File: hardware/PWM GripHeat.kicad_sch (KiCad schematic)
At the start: 21 parts, among them J1 Screw_Terminal_01x02, J2 Screw_Terminal_01x02, Q1 SiS415DNT, Q2 2N7002H

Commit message: Getting there
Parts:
- removed C1, C2, C3, C4, C5: 10uF, Capacitor_SMD:C_0805_2012Metric_Pad1.18x1.45mm_HandSolder, symbol Device:C
- removed C6, C7: EMK325ABJ107MM-T, Capacitor_SMD:C_1210_3225Metric_Pad1.33x2.70mm_HandSolder, symbol Device:C
- removed D1: BZV55B18, Diode_SMD:D_MiniMELF, symbol Diode:BZV55B18
- removed D2: SMAJ24CA, Diode_SMD:D_SMA, symbol Diode:SMAJ24CA
- removed D3: B360, Diode_SMD:D_SMC, symbol Diode:B360
- removed F1: Polyfuse_Small, Fuse:Fuse_2920_7451Metric_Pad2.10x5.45mm_HandSolder, symbol Device:Polyfuse_Small
- removed J2: Screw_Terminal_01x02, TerminalBlock_Phoenix:TerminalBlock_Phoenix_MKDS-1,5-2-5.08_1x02_P5.08mm_Horizontal, symbol Connector:Screw_Terminal_01x02
- removed L1, L2: 100uH, Inductor_SMD:L_Bourns_SRR1260, symbol Device:L
- removed PS1: LM2576HVS-5, Package_TO_SOT_SMD:TO-263-5_TabPin3, symbol Regulator_Switching:LM2576HVS-5
- removed Q1: SiS415DNT, Package_SO:Vishay_PowerPAK_1212-8_Single, symbol Transistor_FET:SiS415DNT
- removed Q2: 2N7002H, Package_TO_SOT_SMD:SOT-23, symbol Transistor_FET:2N7002H
- removed R1: 2.2k, Resistor_SMD:R_1206_3216Metric_Pad1.30x1.75mm_HandSolder, symbol Device:R
- removed R2: 100k, Resistor_SMD:R_1206_3216Metric_Pad1.30x1.75mm_HandSolder, symbol Device:R
- added C10, C12, C8, C9: 10uF, Capacitor_SMD:C_0805_2012Metric_Pad1.18x1.45mm_HandSolder, symbol Device:C
- added C11, C14: 10nF, Capacitor_SMD:C_0805_2012Metric_Pad1.18x1.45mm_HandSolder, symbol Device:C
- added D10, D4, D8, D9: BZV55B5V1, Diode_SMD:D_MiniMELF, symbol Diode:BZV55B5V1
- added D5, D6, D7: BZV55B18, Diode_SMD:D_MiniMELF, symbol Diode:BZV55B18
- added J2: 1770898, TerminalBlock_Phoenix:TerminalBlock_Phoenix_PTSM-0,5-3-2.5-H-THR_1x03_P2.50mm_Horizontal, symbol Connector:Screw_Terminal_01x03
- added J4: 1770924, TerminalBlock_Phoenix:TerminalBlock_Phoenix_PTSM-0,5-6-2.5-H-THR_1x06_P2.50mm_Horizontal, symbol Connector:Screw_Terminal_01x06
- added J5: 0878340619, Connector_IDC:IDC-Header_2x03_P2.54mm_Vertical, symbol Connector_Generic:Conn_02x03_Odd_Even
- added R10, R11: 100k, Resistor_SMD:R_0805_2012Metric_Pad1.20x1.40mm_HandSolder, symbol Device:R
- added R12, R13, R14: 470k, Resistor_SMD:R_0805_2012Metric_Pad1.20x1.40mm_HandSolder, symbol Device:R
- added R4: 100k, Resistor_SMD:R_1206_3216Metric_Pad1.30x1.75mm_HandSolder, symbol Device:R
- added R5, R6, R7, R8: 100R, Resistor_SMD:R_0805_2012Metric_Pad1.20x1.40mm_HandSolder, symbol Device:R
- added R9: 1k, Resistor_SMD:R_0805_2012Metric_Pad1.20x1.40mm_HandSolder, symbol Device:R
- added TP4: SW_IN, TestPoint:TestPoint_Pad_D1.5mm, symbol Connector:TestPoint
- added TP5: RED, TestPoint:TestPoint_Pad_D1.5mm, symbol Connector:TestPoint
- added TP6: GREEN, TestPoint:TestPoint_Pad_D1.5mm, symbol Connector:TestPoint
- added TP7: BLUE, TestPoint:TestPoint_Pad_D1.5mm, symbol Connector:TestPoint
- added TP8: TestPoint, TestPoint:TestPoint_Pad_D1.5mm, symbol Connector:TestPoint
- added U1: ATtiny85-20P, Package_DIP:DIP-8_W7.62mm, symbol MCU_Microchip_ATtiny:ATtiny85-20P
- added U2: SiA462DJ, Package_TO_SOT_SMD:Vishay_PowerPAK_SC70-6L_Single, symbol Transistor_FET:SiA462DJ
- added U3: LM324, Package_SO:SOIC-14_3.9x8.7mm_P1.27mm, symbol Amplifier_Operational:LM324
- J1: value Screw_Terminal_01x02 -> 1770885; footprint TerminalBlock_Phoenix:TerminalBlock_Phoenix_MKDS-1,5-2-5.08_1x02_P5.08mm_Horizontal -> TerminalBlock_Phoenix:TerminalBlock_Phoenix_PTSM-0,5-2-2.5-H-THR_1x02_P2.50mm_Horizontal
- R3: value 100k -> 470k; footprint Resistor_SMD:R_1206_3216Metric_Pad1.30x1.75mm_HandSolder -> Resistor_SMD:R_0805_2012Metric_Pad1.20x1.40mm_HandSolder
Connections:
- net +5V: now also C10.2, C11.2, C12.2, C9.2, J5.2 (Pin_2), R10.1, U1.8 (VCC), U3.4 (V+)
- net +BATT: now also J1.1 (Pin_1), R9.1
- net GND: now also C10.1, C11.1, C12.1, C14.1, C8.1, C9.1, D10.2 (A), D4.2 (A), D5.2 (A), D6.2 (A), D7.2 (A), D8.2 (A), D9.2 (A), J2.3 (Pin_3), J4.6 (Pin_6), J5.6 (Pin_6), R11.2, R4.2, U1.4 (GND), U2.4 (S), U3.11 (V-); no longer R3.2
- net at J1.2 (Pin_2): now also D7.1 (K), U2.1 (D)
- net +IGN renamed +2V5
- net +2V5: now also C14.2, R10.2, R11.1, R12.1, R13.1, R14.2, U3.10 (+), U3.12 (+), U3.3 (+), U3.5 (+)
- new net: D4.1 (K), R13.2, R5.1, U3.14
- new net: D10.1 (K), R12.2, R7.1, U3.7
- new net: J4.5 (Pin_5), R5.2
- new net: D9.1 (K), R3.2, R6.1, U3.8
- new net: C8.2, D6.1 (K), R8.1, U3.2 (-)
- new net: J4.2 (Pin_2), R8.2
- new net: D5.1 (K), J4.1 (Pin_1), R9.2
- new net: J4.3 (Pin_3), R7.2
- new net: J4.4 (Pin_4), R6.2
- new net BLU: TP7.1, U1.2 (XTAL1/PB3), U3.13 (-)
- new net GRN: J5.3 (Pin_3), TP6.1, U1.7 (PB2), U3.9 (-)
- new net PWM_out: R4.1, TP8.1, U1.3 (XTAL2/PB4), U2.3 (G)
- new net Power/+IGN: J2.1 (Pin_1)
- new net Power/BATT: J2.2 (Pin_2)
- new net RED: J5.1 (Pin_1), TP5.1, U1.6 (PB1), U3.6 (-)
- new net RST: J5.5 (Pin_5), U1.1 (~{RESET}/PB5)
- new net SDO: D8.1 (K), J5.4 (Pin_4), R14.1, TP4.1, U1.5 (AREF/PB0), U3.1
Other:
- added sheet Power (Power.kicad_sch)
- note added: "Attiny85 MCU"
- note added: "Heater PWM"
- note added: "Heater+ Heater-"
- note added: "Hysteresis Vref"
- note added: "IGN+ BATT+ GND"
- note added: "Opamp I/O w/ Hysteresis"
- note added: "Power"
- note added: "Programming headers"
- note added: "To_SW (12V) From_SW (12V) Red_Out (5V) Grn_Out (5V) Blu_Out (5V) GND"
- note removed: "Active 20V clamp"
- note removed: "PS1 is enabled only when IGN is high"
- company: (none) -> atomspring
- title: (none) -> PWM GripHeat

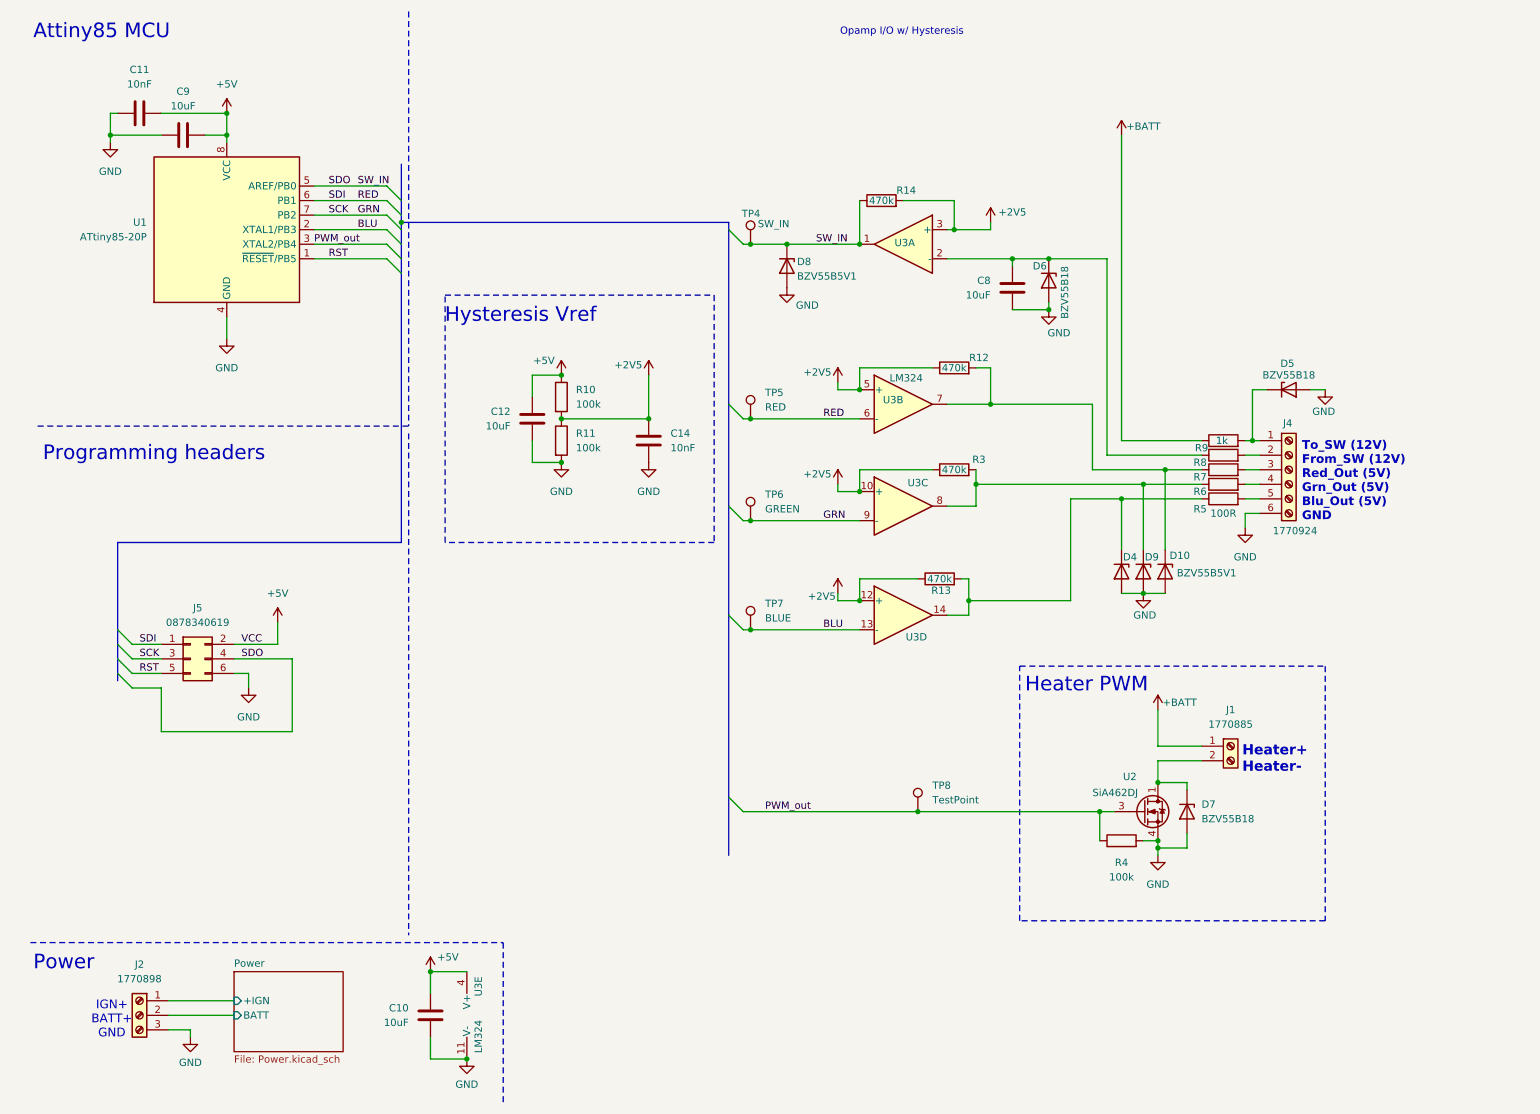
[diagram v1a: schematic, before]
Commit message: PCB Basic outline
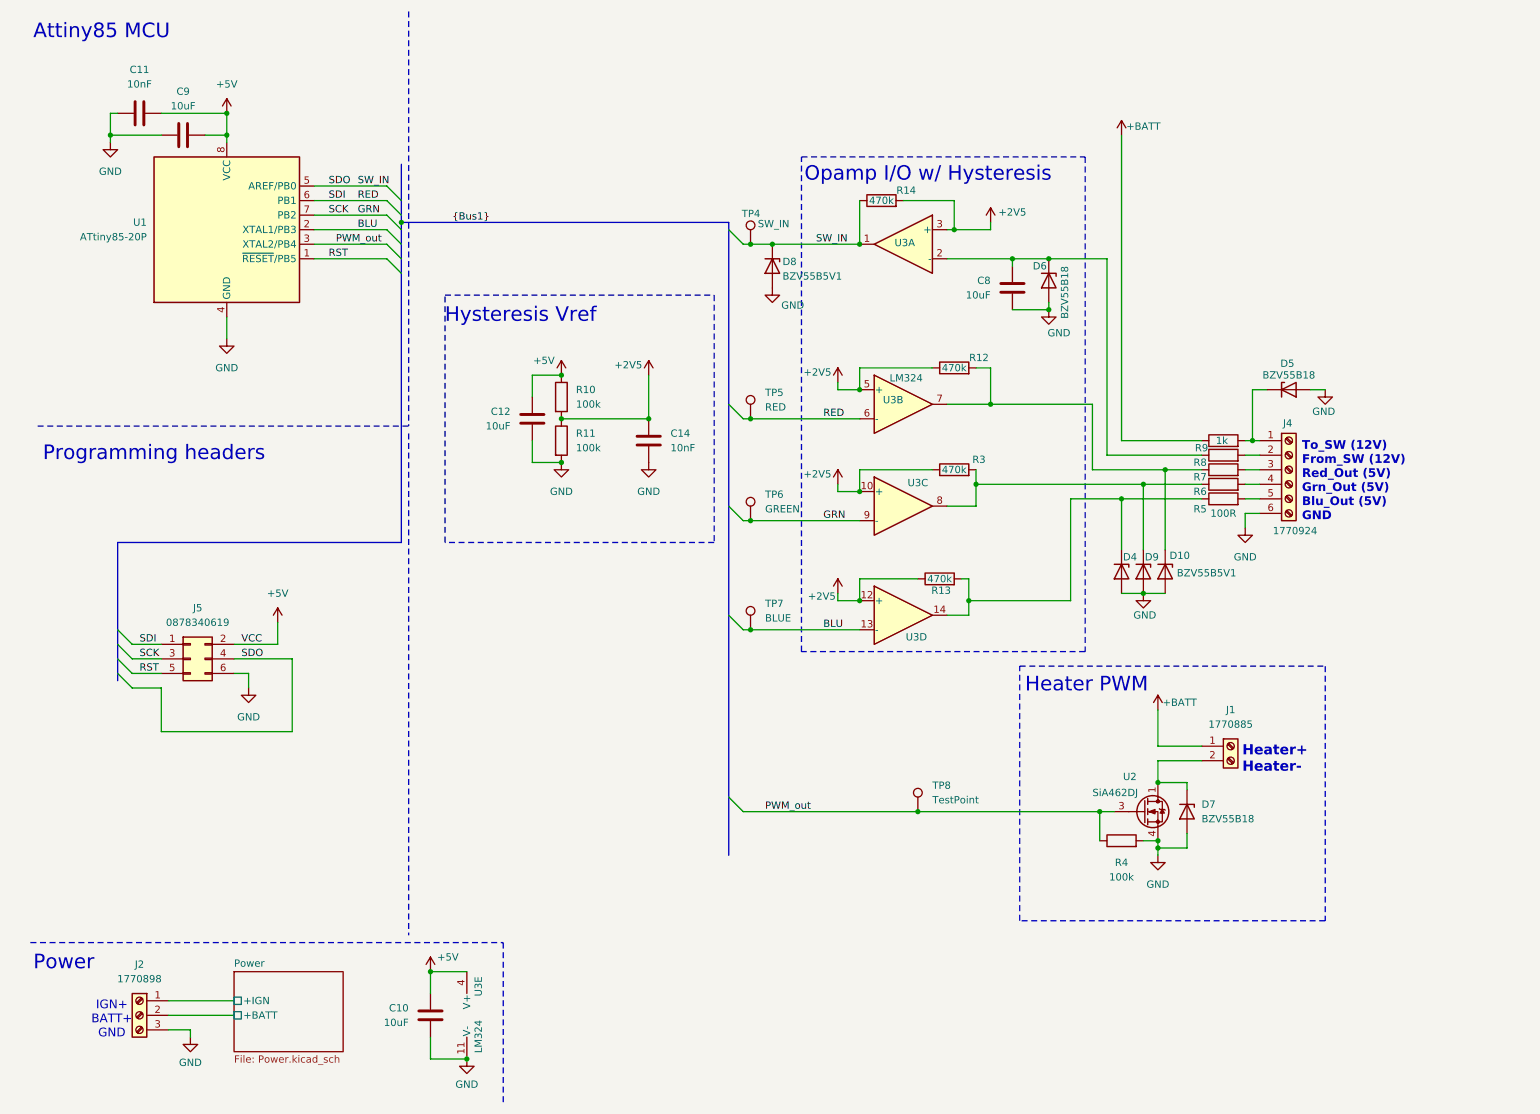
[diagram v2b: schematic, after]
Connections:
- net Power/BATT renamed Power/+BATT
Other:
- sheet Power ports: added +BATT; removed BATT
- moved on the sheet: D8
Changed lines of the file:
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@@
 	)
 	(junction
-		(at 144.78 53.34)
-		(diameter 0)
-		(color 0 0 0 0)
-	)
-	(junction
 		(at 157.48 115.57)
 		(diameter 0)
@@
 	)
 	(junction
+		(at 142.24 53.34)
+		(diameter 0)
+		(color 0 0 0 0)
+	)
+	(junction
 		(at 105.41 76.2)
 		(diameter 0)
@@
 	(wire
 		(pts
+			(xy 142.24 53.34) (xy 157.48 53.34)
+		)
+		(stroke
+			(width 0)
+			(type default)
+		)
+	)
+	(wire
+		(pts
 			(xy 26.67 35.56) (xy 26.67 34.29)
 		)
@@
 	(wire
 		(pts
-			(xy 138.43 53.34) (xy 144.78 53.34)
+			(xy 138.43 53.34) (xy 142.24 53.34)
 		)
 		(stroke
@@
 	(wire
 		(pts
-			(xy 144.78 53.34) (xy 157.48 53.34)
-		)
-		(stroke
-			(width 0)
-			(type default)
-		)
-	)
-	(wire
-		(pts
 			(xy 48.26 125.73) (xy 58.42 125.73)
 		)
@@
 	)
 	(rectangle
+		(start 147.32 38.1)
+		(end 196.85 124.46)
+		(stroke
+			(width 0)
+			(type dot)
+		)
+		(fill
+			(type none)
+		)
+	)
+	(rectangle
 		(start 185.42 127)
 		(end 238.76 171.45)
@@
 	(text "Opamp I/O w/ Hysteresis"
 		(exclude_from_sim no)
-		(at 164.846 16.256 0)
+		(at 169.418 41.148 0)
 		(effects
 			(font
-				(size 1.27 1.27)
+				(size 2.54 2.54)
 			)
 		)
@@
 		)
 	)
+	(label "{Bus1}"
+		(at 86.36 49.53 0)
+		(fields_autoplaced yes)
+		(effects
+			(font
+				(size 1.27 1.27)
+			)
+			(justify left bottom)
+		)
+	)
 	(label "PWM_out"
 		(at 140.97 152.4 0)
@@
 			(font
 				(size 1.27 1.27)
+				(color 132 0 132 1)
 			)
 			(justify left bottom)
@@
 			(font
 				(size 1.27 1.27)
+				(color 132 0 132 1)
 			)
 			(justify left bottom)
@@
 			(font
 				(size 1.27 1.27)
+				(color 132 0 132 1)
 			)
 			(justify left bottom)
@@
 			(font
 				(size 1.27 1.27)
+				(color 132 0 132 1)
 			)
 			(justify left bottom)
@@
 			(font
 				(size 1.27 1.27)
+				(color 132 0 132 1)
 			)
 			(justify left bottom)
@@
 			(font
 				(size 1.27 1.27)
+				(color 132 0 132 1)
 			)
 			(justify left bottom)
@@
 	)
 	(label "PWM_out"
-		(at 62.23 53.34 0)
+		(at 66.04 53.34 0)
 		(fields_autoplaced yes)
 		(effects
@@
 			(font
 				(size 1.27 1.27)
+				(color 132 0 132 1)
 			)
 			(justify left bottom)
@@
 			(font
 				(size 1.27 1.27)
+				(color 132 0 132 1)
 			)
 			(justify left bottom)
@@
 			(font
 				(size 1.27 1.27)
+				(color 132 0 132 1)
 			)
 			(justify left bottom)
@@
 	(symbol
 		(lib_id "Diode:BZV55B5V1")
-		(at 144.78 57.15 270)
+		(at 142.24 57.15 270)
 		(unit 1)
 		(exclude_from_sim no)
@@
 		(dnp no)
 		(property "Reference" "D8"
-			(at 146.558 56.388 90)
+			(at 144.018 56.388 90)
 			(effects
 				(font
@@
 		)
 		(property "Value" "BZV55B5V1"
-			(at 146.558 58.928 90)
+			(at 144.018 58.928 90)
 			(effects
 				(font
@@
 		)
 		(property "Footprint" "Diode_SMD:D_MiniMELF"
-			(at 140.335 57.15 0)
+			(at 137.795 57.15 0)
 			(effects
 				(font
@@
 		)
 		(property "Datasheet" "https://assets.nexperia.com/documents/data-sheet/BZV55_SER.pdf"
-			(at 144.78 57.15 0)
+			(at 142.24 57.15 0)
 			(effects
 				(font
@@
 		)
 		(property "Description" "5.1V, 500mW, 2%, Zener diode, MiniMELF"
-			(at 144.78 57.15 0)
+			(at 142.24 57.15 0)
 			(effects
 				(font
@@
 	(symbol
 		(lib_id "power:GND")
-		(at 144.78 60.96 0)
+		(at 142.24 60.96 0)
 		(unit 1)
 		(exclude_from_sim no)
@@
 		(dnp no)
 		(property "Reference" "#PWR032"
-			(at 144.78 67.31 0)
+			(at 142.24 67.31 0)
 			(effects
 				(font
@@
 		)
 		(property "Value" "GND"
-			(at 148.336 64.008 0)
+			(at 145.796 64.008 0)
 			(effects
 				(font
@@
 		)
 		(property "Footprint" ""
-			(at 144.78 60.96 0)
+			(at 142.24 60.96 0)
 			(effects
 				(font
@@
 		)
 		(property "Datasheet" ""
-			(at 144.78 60.96 0)
+			(at 142.24 60.96 0)
 			(effects
 				(font
@@
 		)
 		(property "Description" "Power symbol creates a global label with name \"GND\" , ground"
-			(at 144.78 60.96 0)
+			(at 142.24 60.96 0)
 			(effects
 				(font
@@
 			)
 		)
-		(pin "BATT" input
+		(pin "+BATT" passive
 			(at 48.26 187.96 180)
 			(effects
@@
 			)
 		)
-		(pin "+IGN" input
+		(pin "+IGN" passive
 			(at 48.26 185.42 180)
 			(effects

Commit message: Pre DRC, almost done!
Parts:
- removed D5: BZV55B18, Diode_SMD:D_MiniMELF, symbol Diode:BZV55B18
- removed J2: 1770898, TerminalBlock_Phoenix:TerminalBlock_Phoenix_PTSM-0,5-3-2.5-H-THR_1x03_P2.50mm_Horizontal, symbol Connector:Screw_Terminal_01x03
- removed J4: 1770924, TerminalBlock_Phoenix:TerminalBlock_Phoenix_PTSM-0,5-6-2.5-H-THR_1x06_P2.50mm_Horizontal, symbol Connector:Screw_Terminal_01x06
- removed J5: 0878340619, Connector_IDC:IDC-Header_2x03_P2.54mm_Vertical, symbol Connector_Generic:Conn_02x03_Odd_Even
- added J2: Screw_Terminal_01x08, Connector_PinHeader_2.54mm:PinHeader_2x04_P2.54mm_Vertical, symbol Connector:Screw_Terminal_01x08
- J1: footprint TerminalBlock_Phoenix:TerminalBlock_Phoenix_PTSM-0,5-2-2.5-H-THR_1x02_P2.50mm_Horizontal -> TerminalBlock:TerminalBlock_MaiXu_MX126-5.0-02P_1x02_P5.00mm
- TP6: value GREEN -> GRN
- TP8: value TestPoint -> PWM
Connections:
- net +BATT: now also J2.1 (Pin_1)
- net GND: now also J2.3 (Pin_3)
- net at R5.2: now also J2.8 (Pin_8)
- net at R8.2: now also J2.5 (Pin_5)
- net at R9.2: now also J2.4 (Pin_4)
- net at R7.2: now also J2.6 (Pin_6)
- net at R6.2: now also J2.7 (Pin_7)
- new net +IGN: J2.2 (Pin_2)
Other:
- note added: "+BATT +IGN GND To_SW (12V) From_SW (12V) Red_Out (5V) Grn_Out (5V) Blu_Out (5V)"
- note removed: "IGN+ BATT+ GND"
- note removed: "Programming headers"
- note removed: "To_SW (12V) From_SW (12V) Red_Out (5V) Grn_Out (5V) Blu_Out (5V) GND"
- moved on the sheet: J1
